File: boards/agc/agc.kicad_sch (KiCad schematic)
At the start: 15 parts, among them J1 Conn_02x31_Top_Bottom, J2 Conn_01x24, J3 Conn_02x13_Top_Bottom, J4 Conn_01x24, U1 LM317L_SO8

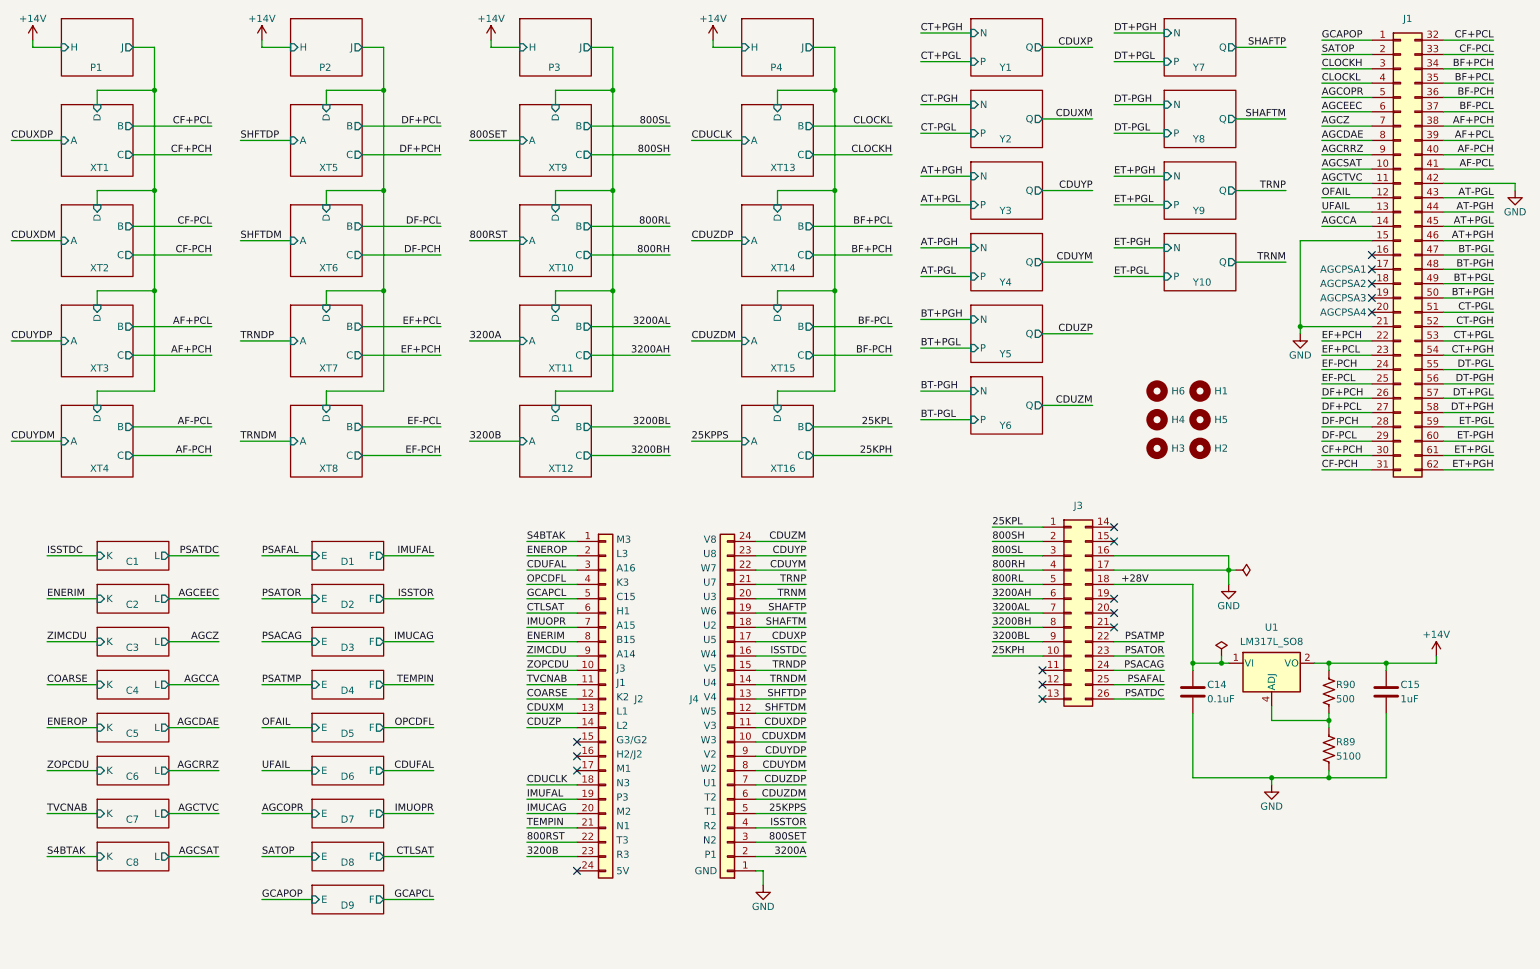
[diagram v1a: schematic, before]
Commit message: Revised AGC board to include RRPONA, RD874, and 28V/14V analog sensing
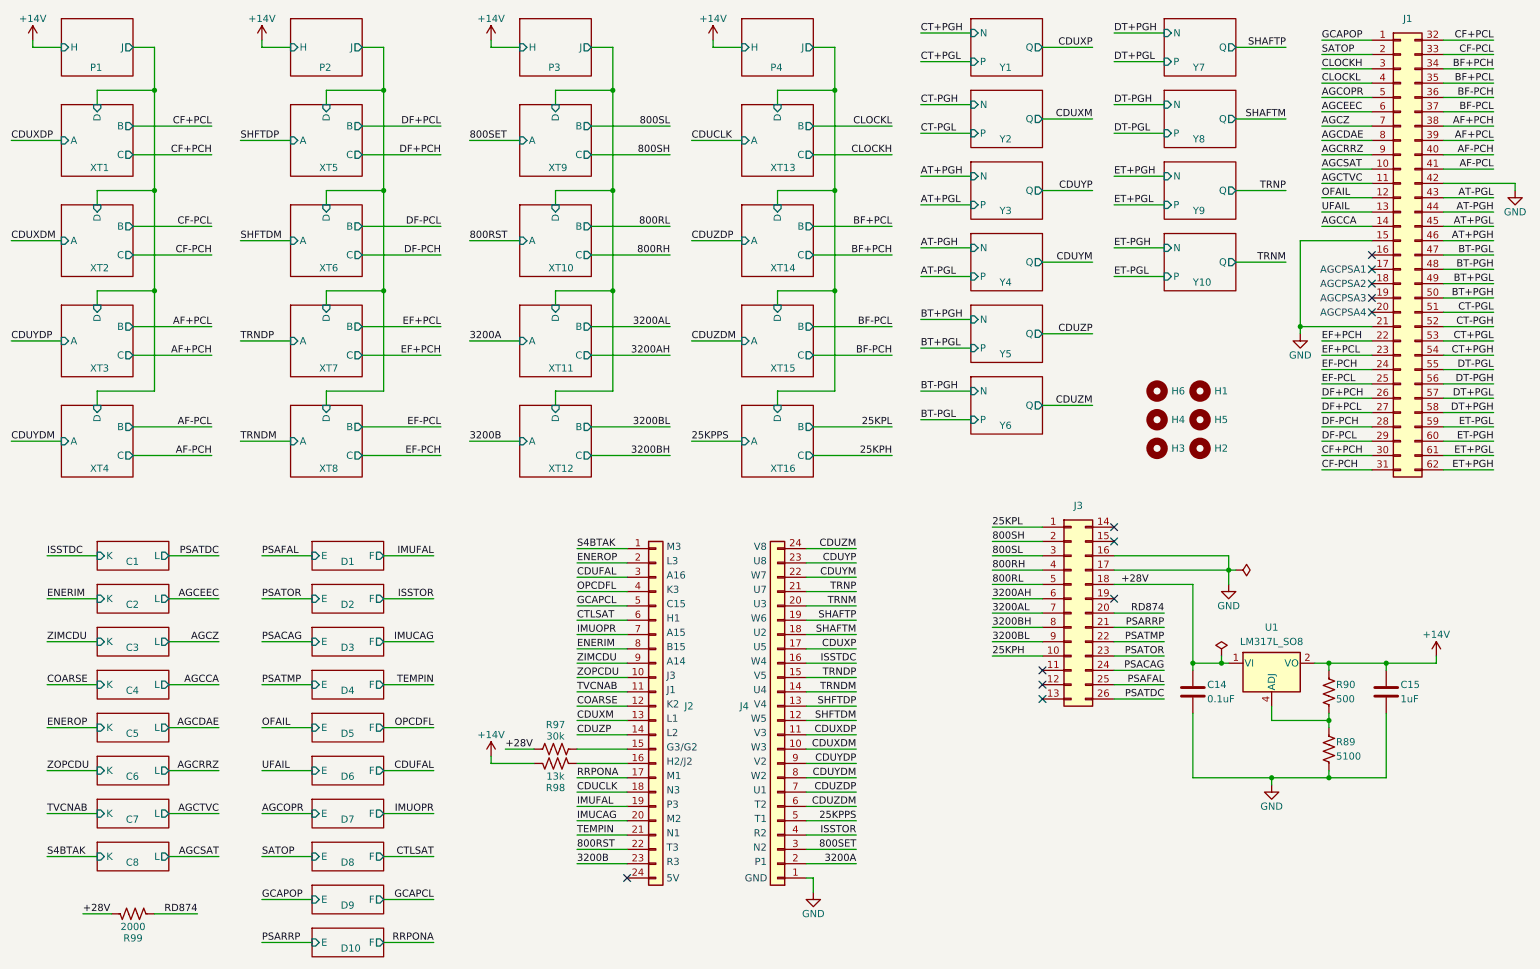
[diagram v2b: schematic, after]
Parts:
- added R97: 30k, Resistor_SMD:R_0603_1608Metric, symbol Device:R_US
- added R98: 13k, Resistor_SMD:R_0603_1608Metric, symbol Device:R_US
- added R99: 2000, Resistor_SMD:R_0603_1608Metric, symbol Device:R_US
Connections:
- net +14V: now also R98.1
- net +28V: now also R97.1, R99.1
- net at J2.15 (Pin_15): now also R97.2
- net at J2.16 (Pin_16): now also R98.2
- net RRPONA: now reaches J2.17 (Pin_17)
- net RD874: now reaches J3.20 (Pin_20)
- net RD874: now also R99.2
- net PSARRP: now reaches J3.21 (Pin_21)
- no-connect marks 17 -> 12
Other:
- added sheet D10 (d1.kicad_sch)
- moved on the sheet: J2, J4
